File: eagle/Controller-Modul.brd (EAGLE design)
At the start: 72 x 49 mm, 36 parts, among them IC3 ATMEGA328P, Q1 BC550C

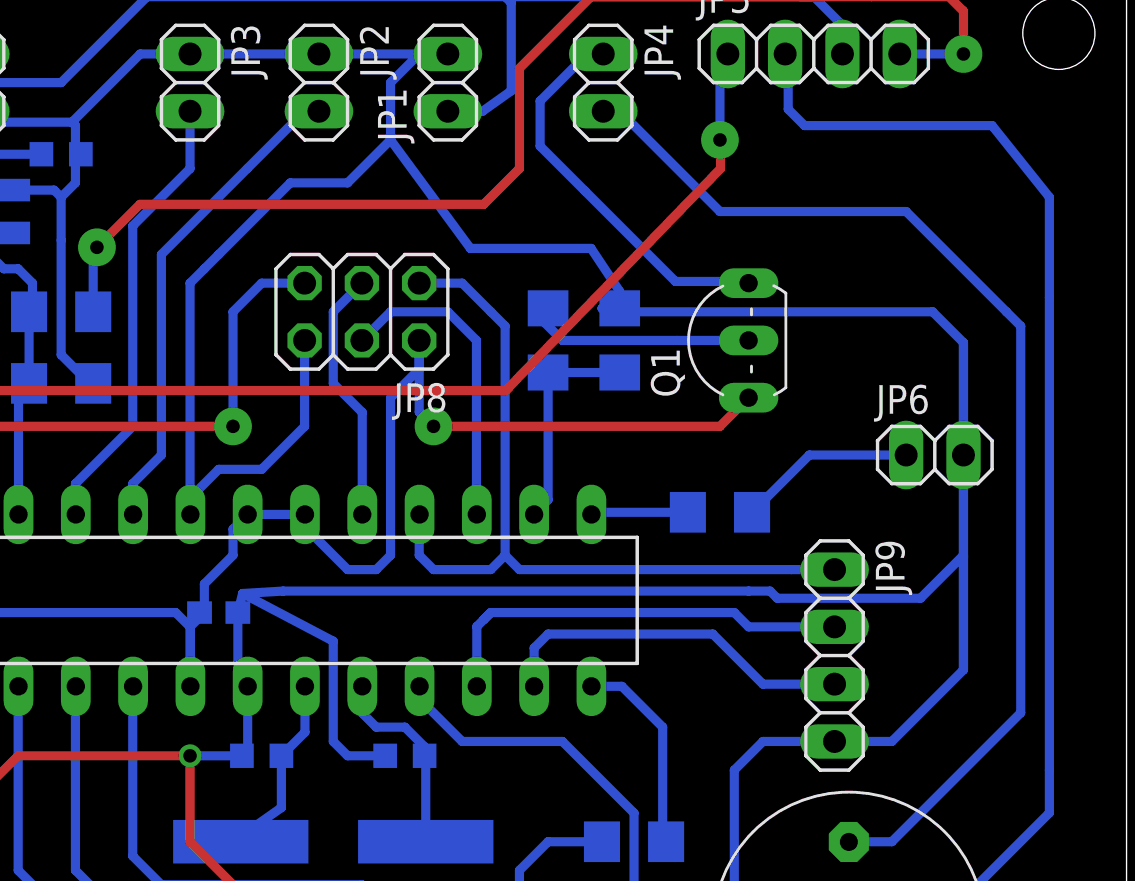
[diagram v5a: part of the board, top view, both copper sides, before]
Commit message: Added forgotten Pull-Down resistors. Lots of new code for executing mosfets
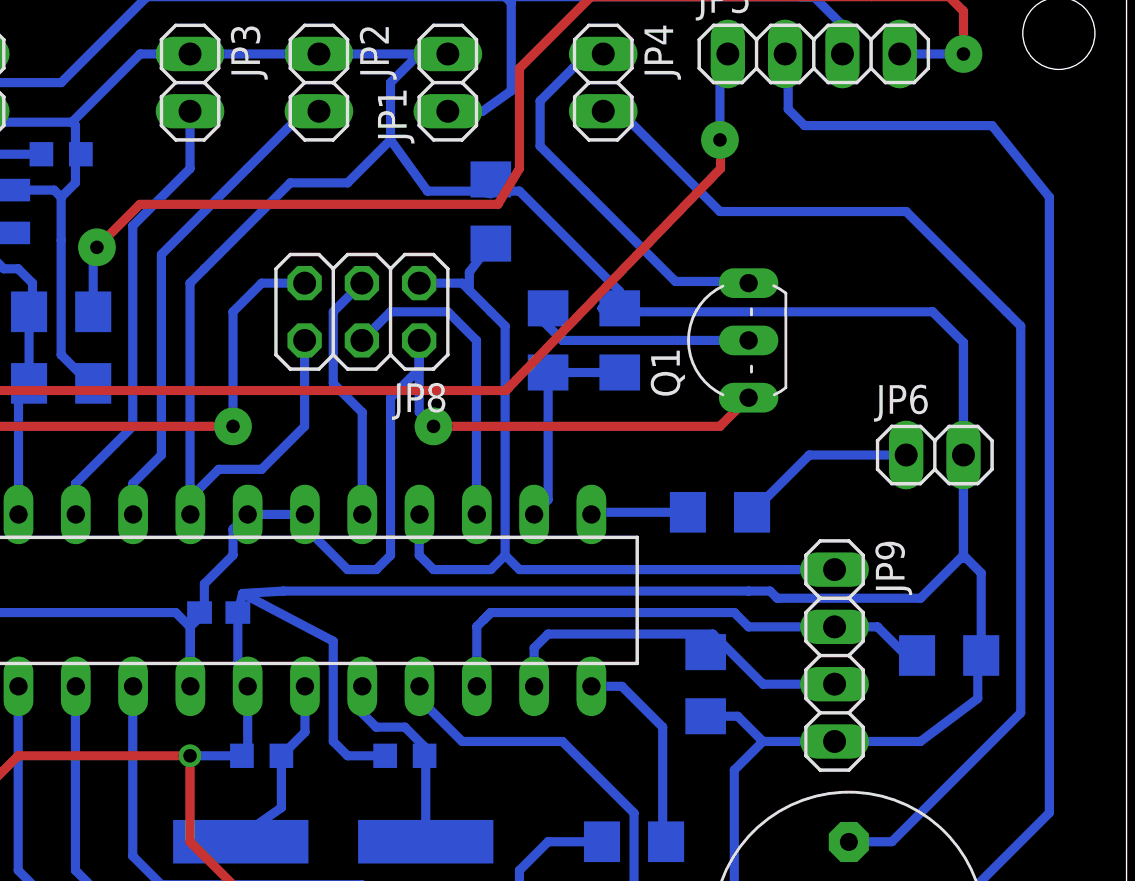
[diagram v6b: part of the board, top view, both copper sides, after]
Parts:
- added R59, R60, R61: 10k, resistor:R1206
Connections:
- removed net N$31: IC3.13, JP9.3
- removed net N$34: IC3.12, JP9.2
- new net FET2: IC3.13, JP9.3, R60.1
- new net FET3: IC3.12, JP9.2, R61.1
- net GND: now also R59.2, R60.2, R61.2
- net MISO: now also R59.1
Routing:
- net FET3: track 0.00 -> 23.7 mm
- net N$34: track 19.5 -> 0.00 mm
- net FET2: track 0.00 -> 17.3 mm
- net N$31: track 16.2 -> 0.00 mm
- net MISO: track 35.8 -> 38.2 mm
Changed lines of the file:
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@@
 <element name="C2" library="rcl" package="C0603K" value="1n" x="24.765" y="40.64" rot="MR0"/>
 <element name="R16" library="resistor" package="R1206" value="3k9" x="24.765" y="33.655" rot="MR0"/>
+<element name="R59" library="resistor" package="R1206" value="10k" x="43.815" y="38.1" rot="MR90"/>
+<element name="R60" library="resistor" package="R1206" value="10k" x="53.34" y="17.145" rot="MR270"/>
+<element name="R61" library="resistor" package="R1206" value="10k" x="64.135" y="18.415" rot="MR180"/>
 </elements>
 <signals>
@@
 <wire x1="39.37" y1="43.815" x2="40.64" y2="45.085" width="0.4064" layer="16"/>
 <wire x1="49.53" y1="33.807" x2="49.53" y2="34.56" width="0.4064" layer="16"/>
-<wire x1="49.53" y1="34.56" x2="48.26" y2="36.465" width="0.4064" layer="16"/>
-<wire x1="48.26" y1="36.465" x2="42.91" y2="36.465" width="0.4064" layer="16"/>
-<wire x1="42.91" y1="36.465" x2="39.37" y2="41.275" width="0.4064" layer="16"/>
+<wire x1="49.53" y1="34.56" x2="45.085" y2="39.005" width="0.4064" layer="16"/>
+<wire x1="45.085" y1="39.005" x2="43.18" y2="39.005" width="0.4064" layer="16"/>
+<wire x1="43.18" y1="39.005" x2="41.005" y2="39.005" width="0.4064" layer="16"/>
+<wire x1="41.005" y1="39.005" x2="39.37" y2="41.275" width="0.4064" layer="16"/>
 <wire x1="20.955" y1="42.545" x2="20.955" y2="42.062" width="0.4064" layer="16"/>
 <wire x1="31.75" y1="36.195" x2="31.115" y2="35.56" width="0.4064" layer="16"/>
@@
 <wire x1="68.58" y1="38.735" x2="66.04" y2="41.91" width="0.4064" layer="16"/>
 <wire x1="64.77" y1="27.305" x2="64.77" y2="32.29" width="0.4064" layer="16"/>
-<wire x1="59.055" y1="14.605" x2="61.595" y2="14.605" width="0.4064" layer="16"/>
-<wire x1="61.595" y1="14.605" x2="64.77" y2="17.78" width="0.4064" layer="16"/>
-<wire x1="64.77" y1="17.78" x2="64.77" y2="22.86" width="0.4064" layer="16"/>
+<wire x1="59.055" y1="14.605" x2="62.865" y2="14.605" width="0.4064" layer="16"/>
+<wire x1="62.865" y1="14.605" x2="65.405" y2="16.51" width="0.4064" layer="16"/>
 <wire x1="64.77" y1="22.86" x2="64.77" y2="22.73" width="0.4064" layer="16"/>
 <wire x1="64.77" y1="22.73" x2="64.77" y2="22.86" width="0.4064" layer="16"/>
@@
 <wire x1="68.58" y1="11.44" x2="59.69" y2="2.55" width="0.4064" layer="16"/>
 <wire x1="64.77" y1="32.29" x2="64.77" y2="22.86" width="0.4064" layer="16"/>
-<wire x1="64.77" y1="22.86" x2="64.77" y2="17.78" width="0.4064" layer="16"/>
 <wire x1="54.61" y1="13.335" x2="54.61" y2="7.63" width="0.4064" layer="16"/>
 <wire x1="54.61" y1="7.63" x2="59.69" y2="2.55" width="0.4064" layer="16"/>
@@
 <wire x1="25.4" y1="39.37" x2="24.765" y2="38.735" width="0.4064" layer="16"/>
 <wire x1="24.765" y1="38.735" x2="24.765" y2="36.83" width="0.4064" layer="16"/>
-<wire x1="8.255" y1="29.058" x2="11.43" y2="29.21" width="0" layer="19" extent="16-16"/>
-<wire x1="3.81" y1="37.465" x2="3.57" y2="37.465" width="0" layer="19" extent="16-16"/>
 <wire x1="22.69" y1="39.05" x2="24.45" y2="39.05" width="0.4064" layer="16"/>
 <wire x1="24.45" y1="39.05" x2="24.765" y2="38.735" width="0.4064" layer="16"/>
+<contactref element="R61" pad="2"/>
+<contactref element="R60" pad="2"/>
+<contactref element="R59" pad="2"/>
+<wire x1="43.815" y1="39.522" x2="43.815" y2="38.887" width="0.4064" layer="16"/>
+<wire x1="43.815" y1="38.887" x2="43.18" y2="39.005" width="0.4064" layer="16"/>
+<wire x1="53.34" y1="15.723" x2="54.762" y2="15.723" width="0.4064" layer="16"/>
+<wire x1="54.762" y1="15.723" x2="55.88" y2="14.605" width="0.4064" layer="16"/>
+<wire x1="65.405" y1="16.51" x2="65.405" y2="18.263" width="0.4064" layer="16"/>
+<wire x1="65.405" y1="18.263" x2="65.557" y2="18.415" width="0.4064" layer="16"/>
+<wire x1="65.557" y1="18.415" x2="65.557" y2="22.073" width="0.4064" layer="16"/>
+<wire x1="65.557" y1="22.073" x2="64.77" y2="22.86" width="0.4064" layer="16"/>
+<wire x1="3.57" y1="37.465" x2="3.81" y2="37.465" width="0" layer="19" extent="16-16"/>
+<wire x1="11.43" y1="29.21" x2="8.255" y2="29.058" width="0" layer="19" extent="16-16"/>
 </signal>
 <signal name="N$6">
@@
 <contactref element="IC3" pad="18"/>
 <wire x1="40.64" y1="34.925" x2="42.545" y2="34.925" width="0.4064" layer="16"/>
-<wire x1="42.545" y1="34.925" x2="43.815" y2="33.655" width="0.4064" layer="16"/>
+<wire x1="42.545" y1="34.925" x2="42.8625" y2="34.6075" width="0.4064" layer="16"/>
+<wire x1="42.8625" y1="34.6075" x2="43.815" y2="33.655" width="0.4064" layer="16"/>
 <wire x1="43.815" y1="33.655" x2="44.45" y2="33.02" width="0.4064" layer="16"/>
 <wire x1="44.45" y1="33.02" x2="44.45" y2="22.86" width="0.4064" layer="16"/>
@@
 <wire x1="57.15" y1="22.225" x2="45.085" y2="22.225" width="0.4064" layer="16"/>
 <wire x1="45.085" y1="22.225" x2="44.45" y2="22.86" width="0.4064" layer="16"/>
+<contactref element="R59" pad="1"/>
+<wire x1="43.815" y1="36.678" x2="42.8625" y2="35.408" width="0.4064" layer="16"/>
+<wire x1="42.8625" y1="35.408" x2="42.8625" y2="34.6075" width="0.4064" layer="16"/>
 </signal>
 <signal name="SCK">
@@
 <wire x1="48.37" y1="24.765" x2="48.275" y2="24.67" width="0.4064" layer="16"/>
 </signal>
-<signal name="N$31">
-<contactref element="IC3" pad="13"/>
-<contactref element="JP9" pad="3"/>
-<wire x1="45.735" y1="17.05" x2="45.735" y2="18.7475" width="0.4064" layer="16"/>
-<wire x1="45.735" y1="18.7475" x2="46.355" y2="19.3675" width="0.4064" layer="16"/>
-<wire x1="46.355" y1="19.3675" x2="53.6575" y2="19.3675" width="0.4064" layer="16"/>
-<wire x1="53.6575" y1="19.3675" x2="55.88" y2="17.145" width="0.4064" layer="16"/>
-<wire x1="55.88" y1="17.145" x2="59.055" y2="17.145" width="0.4064" layer="16"/>
-</signal>
-<signal name="N$34">
-<contactref element="IC3" pad="12"/>
-<contactref element="JP9" pad="2"/>
-<wire x1="43.195" y1="17.05" x2="43.195" y2="19.7" width="0.4064" layer="16"/>
-<wire x1="43.195" y1="19.7" x2="43.4975" y2="20.0025" width="0.4064" layer="16"/>
-<wire x1="43.4975" y1="20.0025" x2="43.815" y2="20.32" width="0.4064" layer="16"/>
-<wire x1="59.055" y1="19.685" x2="55.245" y2="19.685" width="0.4064" layer="16"/>
-<wire x1="55.245" y1="19.685" x2="54.61" y2="20.32" width="0.4064" layer="16"/>
-<wire x1="54.61" y1="20.32" x2="43.815" y2="20.32" width="0.4064" layer="16"/>
-<wire x1="43.815" y1="20.32" x2="43.4975" y2="20.0025" width="0.4064" layer="16"/>
-</signal>
 <signal name="N$10">
 <contactref element="JP2" pad="2"/>
@@
 <via x="26.3525" y="36.5125" extent="1-16" drill="0.6" diameter="1.6764" shape="octagon"/>
 <contactref element="R16" pad="1"/>
-<wire x1="28.2575" y1="38.4175" x2="43.4975" y2="38.4175" width="0.4064" layer="1"/>
-<wire x1="43.4975" y1="38.4175" x2="45.085" y2="40.005" width="0.4064" layer="1"/>
+<wire x1="28.2575" y1="38.4175" x2="44.1325" y2="38.4175" width="0.4064" layer="1"/>
+<wire x1="44.1325" y1="38.4175" x2="45.085" y2="40.005" width="0.4064" layer="1"/>
 <wire x1="45.085" y1="40.005" x2="45.085" y2="44.45" width="0.4064" layer="1"/>
 <wire x1="26.187" y1="33.655" x2="26.187" y2="36.347" width="0.4064" layer="16"/>
@@
 <wire x1="15.385" y1="38.195" x2="14.845" y2="38.735" width="0.4064" layer="16"/>
 </signal>
+<signal name="FET2">
+<contactref element="R60" pad="1"/>
+<contactref element="IC3" pad="13"/>
+<contactref element="JP9" pad="3"/>
+<wire x1="45.735" y1="17.05" x2="45.735" y2="18.7475" width="0.4064" layer="16"/>
+<wire x1="45.735" y1="18.7475" x2="46.355" y2="19.3675" width="0.4064" layer="16"/>
+<wire x1="46.355" y1="19.3675" x2="53.6575" y2="19.3675" width="0.4064" layer="16"/>
+<wire x1="53.6575" y1="19.3675" x2="53.975" y2="19.05" width="0.4064" layer="16"/>
+<wire x1="53.975" y1="19.05" x2="55.88" y2="17.145" width="0.4064" layer="16"/>
+<wire x1="55.88" y1="17.145" x2="59.055" y2="17.145" width="0.4064" layer="16"/>
+<wire x1="53.34" y1="18.567" x2="53.975" y2="18.567" width="0.4064" layer="16"/>
+<wire x1="53.975" y1="18.567" x2="53.975" y2="19.05" width="0.4064" layer="16"/>
+</signal>
+<signal name="FET3">
+<contactref element="R61" pad="1"/>
+<contactref element="IC3" pad="12"/>
+<contactref element="JP9" pad="2"/>
+<wire x1="43.195" y1="17.05" x2="43.195" y2="19.7" width="0.4064" layer="16"/>
+<wire x1="43.195" y1="19.7" x2="43.4975" y2="20.0025" width="0.4064" layer="16"/>
+<wire x1="43.4975" y1="20.0025" x2="43.815" y2="20.32" width="0.4064" layer="16"/>
+<wire x1="59.055" y1="19.685" x2="55.245" y2="19.685" width="0.4064" layer="16"/>
+<wire x1="55.245" y1="19.685" x2="54.61" y2="20.32" width="0.4064" layer="16"/>
+<wire x1="54.61" y1="20.32" x2="43.815" y2="20.32" width="0.4064" layer="16"/>
+<wire x1="43.815" y1="20.32" x2="43.4975" y2="20.0025" width="0.4064" layer="16"/>
+<wire x1="62.713" y1="18.415" x2="62.23" y2="18.415" width="0.4064" layer="16"/>
+<wire x1="62.23" y1="18.415" x2="60.96" y2="19.685" width="0.4064" layer="16"/>
+<wire x1="60.96" y1="19.685" x2="59.055" y2="19.685" width="0.4064" layer="16"/>
+</signal>
+<signal name="N$8">
+</signal>
 </signals>
